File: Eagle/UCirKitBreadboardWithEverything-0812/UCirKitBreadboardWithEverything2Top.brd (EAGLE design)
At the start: 72.8 x 99.4 mm, 600 parts

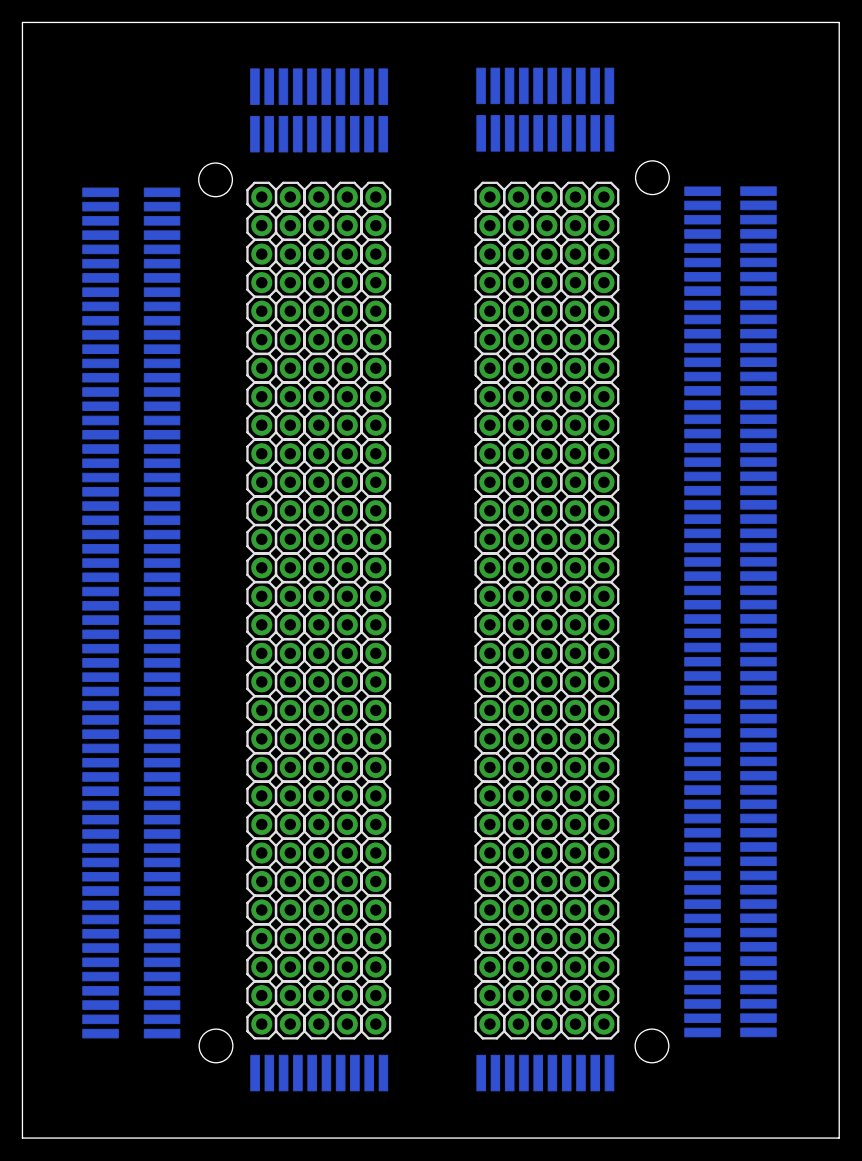
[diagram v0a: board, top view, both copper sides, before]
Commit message: UCirKitEverything2Top is OK for Routing, UCirKitEverything2 is not OK. Look for UCirKitEverything2 for Bottom part
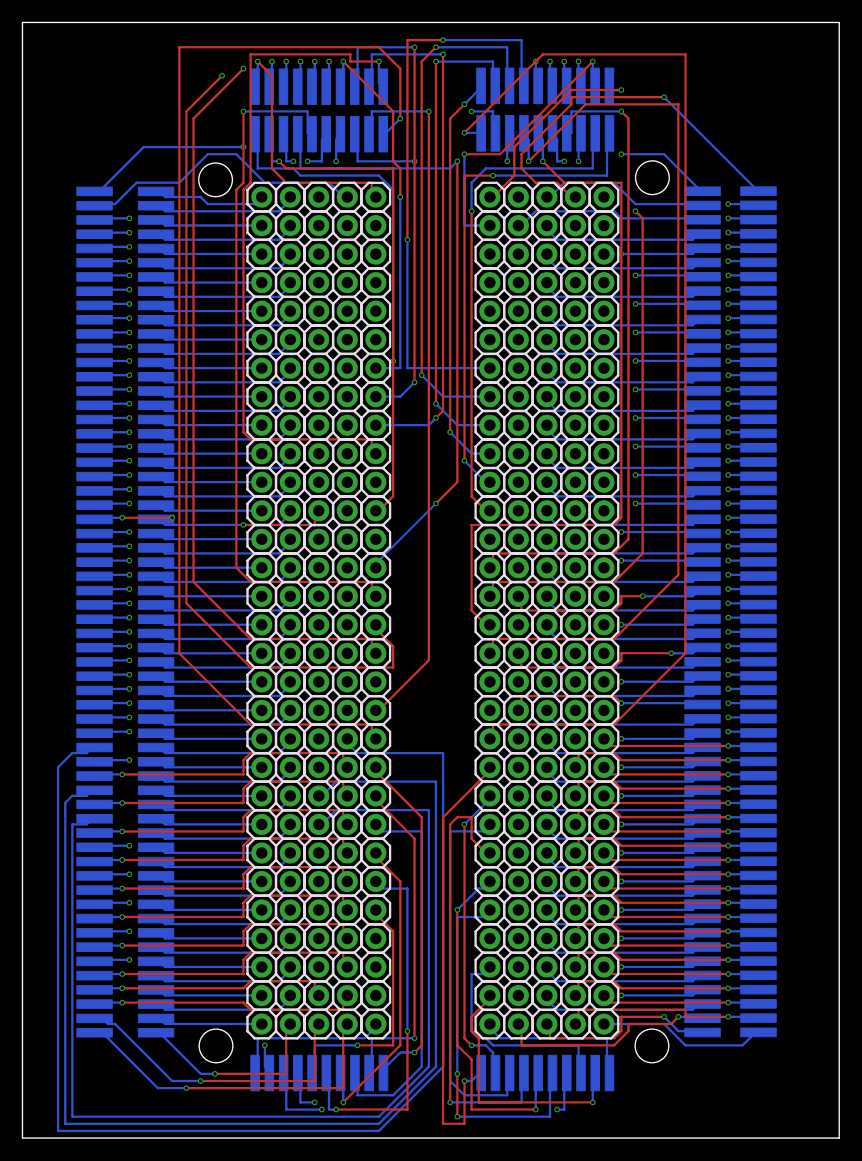
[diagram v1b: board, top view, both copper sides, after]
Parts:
- removed JP1081, JP1082, JP1083, JP1084, JP1085, JP1086, JP1087, JP1088, JP1089, JP1090, JP1091, JP1092, JP1093, JP1094, JP1095, JP1096, JP1097, JP1098, JP1099, JP1100, JP1101, JP1102, JP1103, JP1104, JP1105, JP1106, JP1107, JP1108, JP1109, JP1110, JP1111, JP1112, JP1113, JP1114, JP1115, JP1116, JP1117, JP1118, JP1119, JP1120, JP1121, JP1122, JP1123, JP1124, JP1125, JP1126, JP1127, JP1128, JP1129, JP1130, JP1131, JP1132, JP1133, JP1134, JP1135, JP1136, JP1137, JP1138, JP1139, JP1140, JP901, JP902, JP903, JP904, JP905, JP906, JP907, JP908, JP909, JP910, JP911, JP912, JP913, JP914, JP915, JP916, JP917, JP918, JP919, JP920, JP921, JP922, JP923, JP924, JP925, JP926, JP927, JP928, JP929, JP930, JP931, JP932, JP933, JP934, JP935, JP936, JP937, JP938, JP939, JP940, JP941, JP942, JP943, JP944, JP945, JP946, JP947, JP948, JP949, JP950, JP951, JP952, JP953, JP954, JP955, JP956, JP957, JP958, JP959, JP960: (no value), SparkFun-Connectors:1X01_SMD_3.25X0.85MM_NO_SILK
- added CLEAN300, CLEAN301, CLEAN302, CLEAN303, CLEAN304, CLEAN305, CLEAN306, CLEAN307, CLEAN308, CLEAN309, CLEAN310, CLEAN311, CLEAN312, CLEAN313, CLEAN314, CLEAN315, CLEAN316, CLEAN317, CLEAN318, CLEAN319, CLEAN320, CLEAN321, CLEAN322, CLEAN323, CLEAN324, CLEAN325, CLEAN326, CLEAN327, CLEAN328, CLEAN329, CLEAN330, CLEAN331, CLEAN332, CLEAN333, CLEAN334, CLEAN335, CLEAN336, CLEAN337, CLEAN338, CLEAN339, CLEAN340, CLEAN341, CLEAN342, CLEAN343, CLEAN344, CLEAN345, CLEAN346, CLEAN347, CLEAN348, CLEAN349, CLEAN350, CLEAN351, CLEAN352, CLEAN353, CLEAN354, CLEAN355, CLEAN356, CLEAN357, CLEAN358, CLEAN359, CLEAN480, CLEAN481, CLEAN482, CLEAN483, CLEAN484, CLEAN485, CLEAN486, CLEAN487, CLEAN488, CLEAN489, CLEAN490, CLEAN491, CLEAN492, CLEAN493, CLEAN494, CLEAN495, CLEAN496, CLEAN497, CLEAN498, CLEAN499, CLEAN500, CLEAN501, CLEAN502, CLEAN503, CLEAN504, CLEAN505, CLEAN506, CLEAN507, CLEAN508, CLEAN509, CLEAN510, CLEAN511, CLEAN512, CLEAN513, CLEAN514, CLEAN515, CLEAN516, CLEAN517, CLEAN518, CLEAN519, CLEAN520, CLEAN521, CLEAN522, CLEAN523, CLEAN524, CLEAN525, CLEAN526, CLEAN527, CLEAN528, CLEAN529, CLEAN530, CLEAN531, CLEAN532, CLEAN533, CLEAN534, CLEAN535, CLEAN536, CLEAN537, CLEAN538, CLEAN539: (no value), SparkFun-Connectors:1X01_SMD_3.25X0.85MM_NO_SILK
- renumbered JP1 to CLEAN0, JP10 to CLEAN9, JP100 to CLEAN99, JP1000 to CLEAN399, JP1001 to CLEAN400, JP1002 to CLEAN401, JP1003 to CLEAN402, JP1004 to CLEAN403, JP1005 to CLEAN404, JP1006 to CLEAN405, JP1007 to CLEAN406, JP1008 to CLEAN407, JP1009 to CLEAN408, JP101 to CLEAN100, JP1010 to CLEAN409, JP1011 to CLEAN410, JP1012 to CLEAN411, JP1013 to CLEAN412, JP1014 to CLEAN413, JP1015 to CLEAN414, JP1016 to CLEAN415, JP1017 to CLEAN416, JP1018 to CLEAN417, JP1019 to CLEAN418, JP102 to CLEAN101, JP1020 to CLEAN419, JP1021 to CLEAN420, JP1022 to CLEAN421, JP1023 to CLEAN422, JP1024 to CLEAN423, JP1025 to CLEAN424, JP1026 to CLEAN425, JP1027 to CLEAN426, JP1028 to CLEAN427, JP1029 to CLEAN428, JP103 to CLEAN102, JP1030 to CLEAN429, JP1031 to CLEAN430, JP1032 to CLEAN431, JP1033 to CLEAN432, JP1034 to CLEAN433, JP1035 to CLEAN434, JP1036 to CLEAN435, JP1037 to CLEAN436, JP1038 to CLEAN437, JP1039 to CLEAN438, JP104 to CLEAN103, JP1040 to CLEAN439, JP1041 to CLEAN440, JP1042 to CLEAN441, JP1043 to CLEAN442, JP1044 to CLEAN443, JP1045 to CLEAN444, JP1046 to CLEAN445, JP1047 to CLEAN446, JP1048 to CLEAN447, JP1049 to CLEAN448, JP105 to CLEAN104, JP1050 to CLEAN449, JP1051 to CLEAN450, JP1052 to CLEAN451, JP1053 to CLEAN452, JP1054 to CLEAN453, JP1055 to CLEAN454, JP1056 to CLEAN455, JP1057 to CLEAN456, JP1058 to CLEAN457, JP1059 to CLEAN458, JP106 to CLEAN105, JP1060 to CLEAN459, JP1061 to CLEAN460, JP1062 to CLEAN461, JP1063 to CLEAN462, JP1064 to CLEAN463, JP1065 to CLEAN464, JP1066 to CLEAN465, JP1067 to CLEAN466, JP1068 to CLEAN467, JP1069 to CLEAN468, JP107 to CLEAN106, JP1070 to CLEAN469, JP1071 to CLEAN470, JP1072 to CLEAN471, JP1073 to CLEAN472, JP1074 to CLEAN473, JP1075 to CLEAN474, JP1076 to CLEAN475, JP1077 to CLEAN476, JP1078 to CLEAN477, JP1079 to CLEAN478, JP108 to CLEAN107, JP1080 to CLEAN479, JP109 to CLEAN108, JP11 to CLEAN10, JP110 to CLEAN109, JP111 to CLEAN110, JP112 to CLEAN111, JP113 to CLEAN112, JP114 to CLEAN113, JP1141 to CLEAN540, JP1142 to CLEAN541, JP1143 to CLEAN542, JP1144 to CLEAN543, JP1145 to CLEAN544, JP1146 to CLEAN545, JP1147 to CLEAN546, JP1148 to CLEAN547, JP1149 to CLEAN548, JP115 to CLEAN114, JP1150 to CLEAN549, JP1151 to CLEAN550, JP1152 to CLEAN551, JP1153 to CLEAN552, JP1154 to CLEAN553, JP1155 to CLEAN554, JP1156 to CLEAN555, JP1157 to CLEAN556, JP1158 to CLEAN557, JP1159 to CLEAN558, JP116 to CLEAN115, JP1160 to CLEAN559, JP1161 to CLEAN560, JP1162 to CLEAN561, JP1163 to CLEAN562, JP1164 to CLEAN563, JP1165 to CLEAN564, JP1166 to CLEAN565, JP1167 to CLEAN566, JP1168 to CLEAN567, JP1169 to CLEAN568, JP117 to CLEAN116, JP1170 to CLEAN569, JP1171 to CLEAN570, JP1172 to CLEAN571, JP1173 to CLEAN572, JP1174 to CLEAN573, JP1175 to CLEAN574, JP1176 to CLEAN575, JP1177 to CLEAN576, JP1178 to CLEAN577, JP1179 to CLEAN578, JP118 to CLEAN117, JP1180 to CLEAN579, JP1181 to CLEAN580, JP1182 to CLEAN581, JP1183 to CLEAN582, JP1184 to CLEAN583, JP1185 to CLEAN584, JP1186 to CLEAN585, JP1187 to CLEAN586, JP1188 to CLEAN587, JP1189 to CLEAN588, JP119 to CLEAN118, JP1190 to CLEAN589, JP1191 to CLEAN590, JP1192 to CLEAN591, JP1193 to CLEAN592, JP1194 to CLEAN593, JP1195 to CLEAN594, JP1196 to CLEAN595, JP1197 to CLEAN596, JP1198 to CLEAN597, JP1199 to CLEAN598, JP12 to CLEAN11, JP120 to CLEAN119, JP1200 to CLEAN599, JP121 to CLEAN120, JP122 to CLEAN121, JP123 to CLEAN122, JP124 to CLEAN123, JP125 to CLEAN124, JP126 to CLEAN125, JP127 to CLEAN126, JP128 to CLEAN127, JP129 to CLEAN128, JP13 to CLEAN12, JP130 to CLEAN129, JP131 to CLEAN130, JP132 to CLEAN131, JP133 to CLEAN132, JP134 to CLEAN133, JP135 to CLEAN134, JP136 to CLEAN135, JP137 to CLEAN136, JP138 to CLEAN137, JP139 to CLEAN138, JP14 to CLEAN13, JP140 to CLEAN139, JP141 to CLEAN140, JP142 to CLEAN141, JP143 to CLEAN142, JP144 to CLEAN143, JP145 to CLEAN144, JP146 to CLEAN145, JP147 to CLEAN146, JP148 to CLEAN147, JP149 to CLEAN148, JP15 to CLEAN14, JP150 to CLEAN149, JP151 to CLEAN150, JP152 to CLEAN151, JP153 to CLEAN152, JP154 to CLEAN153, JP155 to CLEAN154, JP156 to CLEAN155, JP157 to CLEAN156, JP158 to CLEAN157, JP159 to CLEAN158, JP16 to CLEAN15, JP160 to CLEAN159, JP161 to CLEAN160, JP162 to CLEAN161, JP163 to CLEAN162, JP164 to CLEAN163, JP165 to CLEAN164, JP166 to CLEAN165, JP167 to CLEAN166, JP168 to CLEAN167, JP169 to CLEAN168, JP17 to CLEAN16, JP170 to CLEAN169, JP171 to CLEAN170, JP172 to CLEAN171, JP173 to CLEAN172, JP174 to CLEAN173, JP175 to CLEAN174, JP176 to CLEAN175, JP177 to CLEAN176, JP178 to CLEAN177, JP179 to CLEAN178, JP18 to CLEAN17, JP180 to CLEAN179, JP181 to CLEAN180, JP182 to CLEAN181, JP183 to CLEAN182, JP184 to CLEAN183, JP185 to CLEAN184, JP186 to CLEAN185, JP187 to CLEAN186, JP188 to CLEAN187, JP189 to CLEAN188, JP19 to CLEAN18, JP190 to CLEAN189, JP191 to CLEAN190, JP192 to CLEAN191, JP193 to CLEAN192, JP194 to CLEAN193, JP195 to CLEAN194, JP196 to CLEAN195, JP197 to CLEAN196, JP198 to CLEAN197, JP199 to CLEAN198, JP2 to CLEAN1, JP20 to CLEAN19, JP200 to CLEAN199, JP201 to CLEAN200, JP202 to CLEAN201, JP203 to CLEAN202, JP204 to CLEAN203, JP205 to CLEAN204, JP206 to CLEAN205, JP207 to CLEAN206, JP208 to CLEAN207, JP209 to CLEAN208, JP21 to CLEAN20, JP210 to CLEAN209, JP211 to CLEAN210, JP212 to CLEAN211, JP213 to CLEAN212, JP214 to CLEAN213, JP215 to CLEAN214, JP216 to CLEAN215, JP217 to CLEAN216, JP218 to CLEAN217, JP219 to CLEAN218, JP22 to CLEAN21, JP220 to CLEAN219, JP221 to CLEAN220, JP222 to CLEAN221, JP223 to CLEAN222, JP224 to CLEAN223, JP225 to CLEAN224, JP226 to CLEAN225, JP227 to CLEAN226, JP228 to CLEAN227, JP229 to CLEAN228, JP23 to CLEAN22, JP230 to CLEAN229, JP231 to CLEAN230, JP232 to CLEAN231, JP233 to CLEAN232, JP234 to CLEAN233, JP235 to CLEAN234, JP236 to CLEAN235, JP237 to CLEAN236, JP238 to CLEAN237, JP239 to CLEAN238, JP24 to CLEAN23, JP240 to CLEAN239, JP241 to CLEAN240, JP242 to CLEAN241, JP243 to CLEAN242, JP244 to CLEAN243, JP245 to CLEAN244, JP246 to CLEAN245, JP247 to CLEAN246, JP248 to CLEAN247, JP249 to CLEAN248, JP25 to CLEAN24, JP250 to CLEAN249, JP251 to CLEAN250, JP252 to CLEAN251, JP253 to CLEAN252, JP254 to CLEAN253, JP255 to CLEAN254, JP256 to CLEAN255, JP257 to CLEAN256, JP258 to CLEAN257, JP259 to CLEAN258, JP26 to CLEAN25, JP260 to CLEAN259, JP261 to CLEAN260, JP262 to CLEAN261, JP263 to CLEAN262, JP264 to CLEAN263, JP265 to CLEAN264, JP266 to CLEAN265, JP267 to CLEAN266, JP268 to CLEAN267, JP269 to CLEAN268, JP27 to CLEAN26, JP270 to CLEAN269, JP271 to CLEAN270, JP272 to CLEAN271, JP273 to CLEAN272, JP274 to CLEAN273, JP275 to CLEAN274, JP276 to CLEAN275, JP277 to CLEAN276, JP278 to CLEAN277, JP279 to CLEAN278, JP28 to CLEAN27, JP280 to CLEAN279, JP281 to CLEAN280, JP282 to CLEAN281, JP283 to CLEAN282, JP284 to CLEAN283, JP285 to CLEAN284, JP286 to CLEAN285, JP287 to CLEAN286, JP288 to CLEAN287, JP289 to CLEAN288, JP29 to CLEAN28, JP290 to CLEAN289, JP291 to CLEAN290, JP292 to CLEAN291, JP293 to CLEAN292, JP294 to CLEAN293, JP295 to CLEAN294, JP296 to CLEAN295, JP297 to CLEAN296, JP298 to CLEAN297, JP299 to CLEAN298, JP3 to CLEAN2, JP30 to CLEAN29, JP300 to CLEAN299, JP31 to CLEAN30, JP32 to CLEAN31, JP33 to CLEAN32, JP34 to CLEAN33, JP35 to CLEAN34, JP36 to CLEAN35, JP37 to CLEAN36, JP38 to CLEAN37, JP39 to CLEAN38, JP4 to CLEAN3, JP40 to CLEAN39, JP41 to CLEAN40, JP42 to CLEAN41, JP43 to CLEAN42, JP44 to CLEAN43, JP45 to CLEAN44, JP46 to CLEAN45, JP47 to CLEAN46, JP48 to CLEAN47, JP49 to CLEAN48, JP5 to CLEAN4, JP50 to CLEAN49, JP51 to CLEAN50, JP52 to CLEAN51, JP53 to CLEAN52, JP54 to CLEAN53, JP55 to CLEAN54, JP56 to CLEAN55, JP57 to CLEAN56, JP58 to CLEAN57, JP59 to CLEAN58, JP6 to CLEAN5, JP60 to CLEAN59, JP61 to CLEAN60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
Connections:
- new net NEW_0: CLEAN360.P$3, CLEAN6.1
- new net NEW_1: CLEAN361.P$3, CLEAN7.1
- new net NEW_10: CLEAN370.P$3, CLEAN56.1
- new net NEW_100: CLEAN208.1, CLEAN460.P$3
- new net NEW_101: CLEAN209.1, CLEAN461.P$3
- new net NEW_102: CLEAN218.1, CLEAN462.P$3
- new net NEW_103: CLEAN219.1, CLEAN463.P$3
- new net NEW_104: CLEAN228.1, CLEAN464.P$3
- new net NEW_105: CLEAN229.1, CLEAN465.P$3
- new net NEW_106: CLEAN238.1, CLEAN466.P$3
- new net NEW_107: CLEAN239.1, CLEAN467.P$3
- new net NEW_108: CLEAN248.1, CLEAN468.P$3
- new net NEW_109: CLEAN249.1, CLEAN469.P$3
- new net NEW_11: CLEAN371.P$3, CLEAN57.1
- new net NEW_110: CLEAN258.1, CLEAN470.P$3
- new net NEW_111: CLEAN259.1, CLEAN471.P$3
- new net NEW_112: CLEAN268.1, CLEAN472.P$3
- new net NEW_113: CLEAN269.1, CLEAN473.P$3
- new net NEW_114: CLEAN278.1, CLEAN474.P$3
- new net NEW_115: CLEAN279.1, CLEAN475.P$3
- new net NEW_116: CLEAN288.1, CLEAN476.P$3
- new net NEW_117: CLEAN289.1, CLEAN477.P$3
- new net NEW_118: CLEAN298.1, CLEAN478.P$3
- new net NEW_119: CLEAN299.1, CLEAN479.P$3
- new net NEW_12: CLEAN372.P$3, CLEAN66.1
- new net NEW_120: CLEAN0.1, CLEAN300.P$3
- new net NEW_121: CLEAN1.1, CLEAN301.P$3
- new net NEW_122: CLEAN10.1, CLEAN302.P$3
- new net NEW_123: CLEAN11.1, CLEAN303.P$3
- new net NEW_124: CLEAN20.1, CLEAN304.P$3
- new net NEW_125: CLEAN21.1, CLEAN305.P$3
- new net NEW_126: CLEAN30.1, CLEAN306.P$3
- new net NEW_127: CLEAN307.P$3, CLEAN31.1
- new net NEW_128: CLEAN308.P$3, CLEAN40.1
- new net NEW_129: CLEAN309.P$3, CLEAN41.1
- new net NEW_13: CLEAN373.P$3, CLEAN67.1
- new net NEW_130: CLEAN310.P$3, CLEAN50.1
- new net NEW_131: CLEAN311.P$3, CLEAN51.1
- new net NEW_132: CLEAN312.P$3, CLEAN60.1
- new net NEW_133: CLEAN313.P$3, CLEAN61.1
- new net NEW_134: CLEAN314.P$3, CLEAN70.1
- new net NEW_135: CLEAN315.P$3, CLEAN71.1
- new net NEW_136: CLEAN316.P$3, CLEAN80.1
- new net NEW_137: CLEAN317.P$3, CLEAN81.1
- new net NEW_138: CLEAN318.P$3, CLEAN90.1
- new net NEW_139: CLEAN319.P$3, CLEAN91.1
- new net NEW_14: CLEAN374.P$3, CLEAN76.1
- new net NEW_140: CLEAN100.1, CLEAN320.P$3
- new net NEW_141: CLEAN101.1, CLEAN321.P$3
- new net NEW_142: CLEAN110.1, CLEAN322.P$3
- new net NEW_143: CLEAN111.1, CLEAN323.P$3
- new net NEW_144: CLEAN120.1, CLEAN324.P$3
- new net NEW_145: CLEAN121.1, CLEAN325.P$3
- new net NEW_146: CLEAN130.1, CLEAN326.P$3
- new net NEW_147: CLEAN131.1, CLEAN327.P$3
- new net NEW_148: CLEAN140.1, CLEAN328.P$3
- new net NEW_149: CLEAN141.1, CLEAN329.P$3
- new net NEW_15: CLEAN375.P$3, CLEAN77.1
- new net NEW_150: CLEAN150.1, CLEAN330.P$3
- new net NEW_151: CLEAN151.1, CLEAN331.P$3
- new net NEW_152: CLEAN160.1, CLEAN332.P$3
- new net NEW_153: CLEAN161.1, CLEAN333.P$3
- new net NEW_154: CLEAN170.1, CLEAN334.P$3
- new net NEW_155: CLEAN171.1, CLEAN335.P$3
- new net NEW_156: CLEAN180.1, CLEAN336.P$3
- new net NEW_157: CLEAN181.1, CLEAN337.P$3
- new net NEW_158: CLEAN190.1, CLEAN338.P$3
- new net NEW_159: CLEAN191.1, CLEAN339.P$3
- new net NEW_16: CLEAN376.P$3, CLEAN86.1
- new net NEW_160: CLEAN200.1, CLEAN340.P$3
- new net NEW_161: CLEAN201.1, CLEAN341.P$3
- new net NEW_162: CLEAN210.1, CLEAN342.P$3
- new net NEW_163: CLEAN211.1, CLEAN343.P$3
- new net NEW_164: CLEAN220.1, CLEAN344.P$3
- new net NEW_165: CLEAN221.1, CLEAN345.P$3
- new net NEW_166: CLEAN230.1, CLEAN346.P$3
- new net NEW_167: CLEAN231.1, CLEAN347.P$3
- new net NEW_168: CLEAN240.1, CLEAN348.P$3
- new net NEW_169: CLEAN241.1, CLEAN349.P$3
- new net NEW_17: CLEAN377.P$3, CLEAN87.1
- new net NEW_170: CLEAN250.1, CLEAN350.P$3
- new net NEW_171: CLEAN251.1, CLEAN351.P$3
- new net NEW_172: CLEAN260.1, CLEAN352.P$3
- new net NEW_173: CLEAN261.1, CLEAN353.P$3
- new net NEW_174: CLEAN270.1, CLEAN354.P$3
- new net NEW_175: CLEAN271.1, CLEAN355.P$3
- new net NEW_176: CLEAN280.1, CLEAN356.P$3
- new net NEW_177: CLEAN281.1, CLEAN357.P$3
- new net NEW_178: CLEAN290.1, CLEAN358.P$3
- new net NEW_179: CLEAN291.1, CLEAN359.P$3
- new net NEW_18: CLEAN378.P$3, CLEAN96.1
- new net NEW_180: CLEAN2.1, CLEAN480.P$3
- new net NEW_181: CLEAN3.1, CLEAN481.P$3
- new net NEW_182: CLEAN12.1, CLEAN482.P$3
- new net NEW_183: CLEAN13.1, CLEAN483.P$3
- new net NEW_184: CLEAN22.1, CLEAN484.P$3
- new net NEW_185: CLEAN23.1, CLEAN485.P$3
- new net NEW_186: CLEAN32.1, CLEAN486.P$3
- new net NEW_187: CLEAN33.1, CLEAN487.P$3
- new net NEW_188: CLEAN42.1, CLEAN488.P$3
- new net NEW_189: CLEAN43.1, CLEAN489.P$3
- new net NEW_19: CLEAN379.P$3, CLEAN97.1
- new net NEW_190: CLEAN490.P$3, CLEAN52.1
- new net NEW_191: CLEAN491.P$3, CLEAN53.1
- new net NEW_192: CLEAN492.P$3, CLEAN62.1
- new net NEW_193: CLEAN493.P$3, CLEAN63.1
- new net NEW_194: CLEAN494.P$3, CLEAN72.1
- new net NEW_195: CLEAN495.P$3, CLEAN73.1
- new net NEW_196: CLEAN496.P$3, CLEAN82.1
- new net NEW_197: CLEAN497.P$3, CLEAN83.1
- new net NEW_198: CLEAN498.P$3, CLEAN92.1
- new net NEW_199: CLEAN499.P$3, CLEAN93.1
- new net NEW_2: CLEAN16.1, CLEAN362.P$3
- new net NEW_20: CLEAN106.1, CLEAN380.P$3
- new net NEW_200: CLEAN102.1, CLEAN500.P$3
- new net NEW_201: CLEAN103.1, CLEAN501.P$3
- new net NEW_202: CLEAN112.1, CLEAN502.P$3
- new net NEW_203: CLEAN113.1, CLEAN503.P$3
- new net NEW_204: CLEAN122.1, CLEAN504.P$3
- new net NEW_205: CLEAN123.1, CLEAN505.P$3
- new net NEW_206: CLEAN132.1, CLEAN506.P$3
- new net NEW_207: CLEAN133.1, CLEAN507.P$3
- new net NEW_208: CLEAN142.1, CLEAN508.P$3
- new net NEW_209: CLEAN143.1, CLEAN509.P$3
- new net NEW_21: CLEAN107.1, CLEAN381.P$3
- new net NEW_210: CLEAN152.1, CLEAN510.P$3
- new net NEW_211: CLEAN153.1, CLEAN511.P$3
- new net NEW_212: CLEAN162.1, CLEAN512.P$3
- new net NEW_213: CLEAN163.1, CLEAN513.P$3
- new net NEW_214: CLEAN172.1, CLEAN514.P$3
- new net NEW_215: CLEAN173.1, CLEAN515.P$3
- new net NEW_216: CLEAN182.1, CLEAN516.P$3
- new net NEW_217: CLEAN183.1, CLEAN517.P$3
- new net NEW_218: CLEAN192.1, CLEAN518.P$3
- new net NEW_219: CLEAN193.1, CLEAN519.P$3
- new net NEW_22: CLEAN116.1, CLEAN382.P$3
- new net NEW_220: CLEAN202.1, CLEAN520.P$3
- new net NEW_221: CLEAN203.1, CLEAN521.P$3
- new net NEW_222: CLEAN212.1, CLEAN522.P$3
- new net NEW_223: CLEAN213.1, CLEAN523.P$3
- new net NEW_224: CLEAN222.1, CLEAN524.P$3
- new net NEW_225: CLEAN223.1, CLEAN525.P$3
- new net NEW_226: CLEAN232.1, CLEAN526.P$3
- new net NEW_227: CLEAN233.1, CLEAN527.P$3
- new net NEW_228: CLEAN242.1, CLEAN528.P$3
- new net NEW_229: CLEAN243.1, CLEAN529.P$3
- new net NEW_23: CLEAN117.1, CLEAN383.P$3
- new net NEW_230: CLEAN252.1, CLEAN530.P$3
- new net NEW_231: CLEAN253.1, CLEAN531.P$3
- new net NEW_232: CLEAN262.1, CLEAN532.P$3
- new net NEW_233: CLEAN263.1, CLEAN533.P$3
- new net NEW_234: CLEAN272.1, CLEAN534.P$3
- new net NEW_235: CLEAN273.1, CLEAN535.P$3
- new net NEW_236: CLEAN282.1, CLEAN536.P$3
- new net NEW_237: CLEAN283.1, CLEAN537.P$3
- new net NEW_238: CLEAN292.1, CLEAN538.P$3
- new net NEW_239: CLEAN293.1, CLEAN539.P$3
- new net NEW_24: CLEAN126.1, CLEAN384.P$3
- new net NEW_240: CLEAN4.1, CLEAN560.P$3
- new net NEW_241: CLEAN14.1, CLEAN561.P$3
- new net NEW_242: CLEAN24.1, CLEAN562.P$3
- new net NEW_243: CLEAN34.1, CLEAN563.P$3
- new net NEW_244: CLEAN44.1, CLEAN564.P$3
- new net NEW_245: CLEAN54.1, CLEAN565.P$3
- new net NEW_246: CLEAN566.P$3, CLEAN64.1
- new net NEW_247: CLEAN567.P$3, CLEAN74.1
- new net NEW_248: CLEAN568.P$3, CLEAN84.1
- new net NEW_249: CLEAN569.P$3, CLEAN94.1
- new net NEW_25: CLEAN127.1, CLEAN385.P$3
- new net NEW_250: CLEAN104.1, CLEAN570.P$3
- new net NEW_251: CLEAN114.1, CLEAN571.P$3
- new net NEW_252: CLEAN124.1, CLEAN572.P$3
- new net NEW_253: CLEAN134.1, CLEAN573.P$3
- new net NEW_254: CLEAN144.1, CLEAN574.P$3
- new net NEW_255: CLEAN154.1, CLEAN575.P$3
- new net NEW_256: CLEAN164.1, CLEAN576.P$3
- new net NEW_257: CLEAN174.1, CLEAN577.P$3
- new net NEW_258: CLEAN184.1, CLEAN578.P$3
- new net NEW_259: CLEAN194.1, CLEAN579.P$3
- new net NEW_26: CLEAN136.1, CLEAN386.P$3
- new net NEW_260: CLEAN294.1, CLEAN590.P$3
- new net NEW_261: CLEAN284.1, CLEAN591.P$3
- new net NEW_262: CLEAN274.1, CLEAN592.P$3
- new net NEW_263: CLEAN264.1, CLEAN593.P$3
- new net NEW_264: CLEAN254.1, CLEAN594.P$3
- new net NEW_265: CLEAN244.1, CLEAN595.P$3
- new net NEW_266: CLEAN234.1, CLEAN596.P$3
- new net NEW_267: CLEAN224.1, CLEAN597.P$3
- new net NEW_268: CLEAN214.1, CLEAN598.P$3
- new net NEW_269: CLEAN204.1, CLEAN599.P$3
- new net NEW_27: CLEAN137.1, CLEAN387.P$3
- new net NEW_270: CLEAN195.1, CLEAN540.P$3
- new net NEW_271: CLEAN185.1, CLEAN541.P$3
- new net NEW_272: CLEAN175.1, CLEAN542.P$3
- new net NEW_273: CLEAN165.1, CLEAN543.P$3
- new net NEW_274: CLEAN155.1, CLEAN544.P$3
- new net NEW_275: CLEAN145.1, CLEAN545.P$3
- new net NEW_276: CLEAN135.1, CLEAN546.P$3
- new net NEW_277: CLEAN125.1, CLEAN547.P$3
- new net NEW_278: CLEAN115.1, CLEAN548.P$3
- new net NEW_279: CLEAN105.1, CLEAN549.P$3
- new net NEW_28: CLEAN146.1, CLEAN388.P$3
- new net NEW_280: CLEAN550.P$3, CLEAN95.1
- new net NEW_281: CLEAN551.P$3, CLEAN85.1
- new net NEW_282: CLEAN552.P$3, CLEAN75.1
- new net NEW_283: CLEAN553.P$3, CLEAN65.1
- new net NEW_284: CLEAN55.1, CLEAN554.P$3
- new net NEW_285: CLEAN45.1, CLEAN555.P$3
- new net NEW_286: CLEAN35.1, CLEAN556.P$3
- new net NEW_287: CLEAN25.1, CLEAN557.P$3
- new net NEW_288: CLEAN15.1, CLEAN558.P$3
- new net NEW_289: CLEAN5.1, CLEAN559.P$3
- new net NEW_29: CLEAN147.1, CLEAN389.P$3
- new net NEW_290: CLEAN205.1, CLEAN580.P$3
- new net NEW_291: CLEAN215.1, CLEAN581.P$3
- new net NEW_292: CLEAN225.1, CLEAN582.P$3
- new net NEW_293: CLEAN235.1, CLEAN583.P$3
- new net NEW_294: CLEAN245.1, CLEAN584.P$3
- new net NEW_295: CLEAN255.1, CLEAN585.P$3
- new net NEW_296: CLEAN265.1, CLEAN586.P$3
- new net NEW_297: CLEAN275.1, CLEAN587.P$3
- new net NEW_298: CLEAN285.1, CLEAN588.P$3
- new net NEW_299: CLEAN295.1, CLEAN589.P$3
- new net NEW_3: CLEAN17.1, CLEAN363.P$3
- new net NEW_30: CLEAN156.1, CLEAN390.P$3
- new net NEW_31: CLEAN157.1, CLEAN391.P$3
- new net NEW_32: CLEAN166.1, CLEAN392.P$3
- new net NEW_33: CLEAN167.1, CLEAN393.P$3
- new net NEW_34: CLEAN176.1, CLEAN394.P$3
- new net NEW_35: CLEAN177.1, CLEAN395.P$3
- new net NEW_36: CLEAN186.1, CLEAN396.P$3
- new net NEW_37: CLEAN187.1, CLEAN397.P$3
- new net NEW_38: CLEAN196.1, CLEAN398.P$3
- new net NEW_39: CLEAN197.1, CLEAN399.P$3
- new net NEW_4: CLEAN26.1, CLEAN364.P$3
- new net NEW_40: CLEAN206.1, CLEAN400.P$3
- new net NEW_41: CLEAN207.1, CLEAN401.P$3
- new net NEW_42: CLEAN216.1, CLEAN402.P$3
- new net NEW_43: CLEAN217.1, CLEAN403.P$3
- new net NEW_44: CLEAN226.1, CLEAN404.P$3
- new net NEW_45: CLEAN227.1, CLEAN405.P$3
- new net NEW_46: CLEAN236.1, CLEAN406.P$3
- new net NEW_47: CLEAN237.1, CLEAN407.P$3
- new net NEW_48: CLEAN246.1, CLEAN408.P$3
- new net NEW_49: CLEAN247.1, CLEAN409.P$3
- new net NEW_5: CLEAN27.1, CLEAN365.P$3
- new net NEW_50: CLEAN256.1, CLEAN410.P$3
- new net NEW_51: CLEAN257.1, CLEAN411.P$3
- new net NEW_52: CLEAN266.1, CLEAN412.P$3
- new net NEW_53: CLEAN267.1, CLEAN413.P$3
- new net NEW_54: CLEAN276.1, CLEAN414.P$3
- new net NEW_55: CLEAN277.1, CLEAN415.P$3
- new net NEW_56: CLEAN286.1, CLEAN416.P$3
- new net NEW_57: CLEAN287.1, CLEAN417.P$3
- new net NEW_58: CLEAN296.1, CLEAN418.P$3
- new net NEW_59: CLEAN297.1, CLEAN419.P$3
- new net NEW_6: CLEAN36.1, CLEAN366.P$3
- new net NEW_60: CLEAN420.P$3, CLEAN8.1
- new net NEW_61: CLEAN421.P$3, CLEAN9.1
- new net NEW_62: CLEAN18.1, CLEAN422.P$3
- new net NEW_63: CLEAN19.1, CLEAN423.P$3
- new net NEW_64: CLEAN28.1, CLEAN424.P$3
- new net NEW_65: CLEAN29.1, CLEAN425.P$3
- new net NEW_66: CLEAN38.1, CLEAN426.P$3
- new net NEW_67: CLEAN39.1, CLEAN427.P$3
- new net NEW_68: CLEAN428.P$3, CLEAN48.1
- new net NEW_69: CLEAN429.P$3, CLEAN49.1
- new net NEW_7: CLEAN367.P$3, CLEAN37.1
- new net NEW_70: CLEAN430.P$3, CLEAN58.1
- new net NEW_71: CLEAN431.P$3, CLEAN59.1
- new net NEW_72: CLEAN432.P$3, CLEAN68.1
- new net NEW_73: CLEAN433.P$3, CLEAN69.1
- new net NEW_74: CLEAN434.P$3, CLEAN78.1
- new net NEW_75: CLEAN435.P$3, CLEAN79.1
- new net NEW_76: CLEAN436.P$3, CLEAN88.1
- new net NEW_77: CLEAN437.P$3, CLEAN89.1
- new net NEW_78: CLEAN438.P$3, CLEAN98.1
- new net NEW_79: CLEAN439.P$3, CLEAN99.1
- new net NEW_8: CLEAN368.P$3, CLEAN46.1
- new net NEW_80: CLEAN108.1, CLEAN440.P$3
- new net NEW_81: CLEAN109.1, CLEAN441.P$3
- new net NEW_82: CLEAN118.1, CLEAN442.P$3
- new net NEW_83: CLEAN119.1, CLEAN443.P$3
- new net NEW_84: CLEAN128.1, CLEAN444.P$3
- new net NEW_85: CLEAN129.1, CLEAN445.P$3
- new net NEW_86: CLEAN138.1, CLEAN446.P$3
- new net NEW_87: CLEAN139.1, CLEAN447.P$3
- new net NEW_88: CLEAN148.1, CLEAN448.P$3
- new net NEW_89: CLEAN149.1, CLEAN449.P$3
- new net NEW_9: CLEAN369.P$3, CLEAN47.1
- new net NEW_90: CLEAN158.1, CLEAN450.P$3
- new net NEW_91: CLEAN159.1, CLEAN451.P$3
- new net NEW_92: CLEAN168.1, CLEAN452.P$3
- new net NEW_93: CLEAN169.1, CLEAN453.P$3
- new net NEW_94: CLEAN178.1, CLEAN454.P$3
- new net NEW_95: CLEAN179.1, CLEAN455.P$3
- new net NEW_96: CLEAN188.1, CLEAN456.P$3
- new net NEW_97: CLEAN189.1, CLEAN457.P$3
- new net NEW_98: CLEAN198.1, CLEAN458.P$3
- new net NEW_99: CLEAN199.1, CLEAN459.P$3
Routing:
- net NEW_219: track 0.00 -> 110.3 mm
- net NEW_222: track 0.00 -> 103.3 mm
- net NEW_259: track 0.00 -> 102.4 mm, vias 0 -> 1
- net NEW_270: track 0.00 -> 98.7 mm, vias 0 -> 1
- net NEW_224: track 0.00 -> 95.1 mm
- net NEW_255: track 0.00 -> 88.1 mm, vias 0 -> 2
- net NEW_256: track 0.00 -> 81.4 mm, vias 0 -> 2
- net NEW_273: track 0.00 -> 80.4 mm, vias 0 -> 1
- net NEW_274: track 0.00 -> 63.6 mm, vias 0 -> 1
- net NEW_254: track 0.00 -> 63.2 mm, vias 0 -> 1
- net NEW_258: track 0.00 -> 62.7 mm, vias 0 -> 1
- net NEW_249: track 0.00 -> 61.7 mm, vias 0 -> 1
- net NEW_271: track 0.00 -> 60.4 mm, vias 0 -> 1
- net NEW_276: track 0.00 -> 59.3 mm, vias 0 -> 1
- net NEW_275: track 0.00 -> 58.1 mm, vias 0 -> 2
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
